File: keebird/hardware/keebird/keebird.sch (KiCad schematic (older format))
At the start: 2 parts

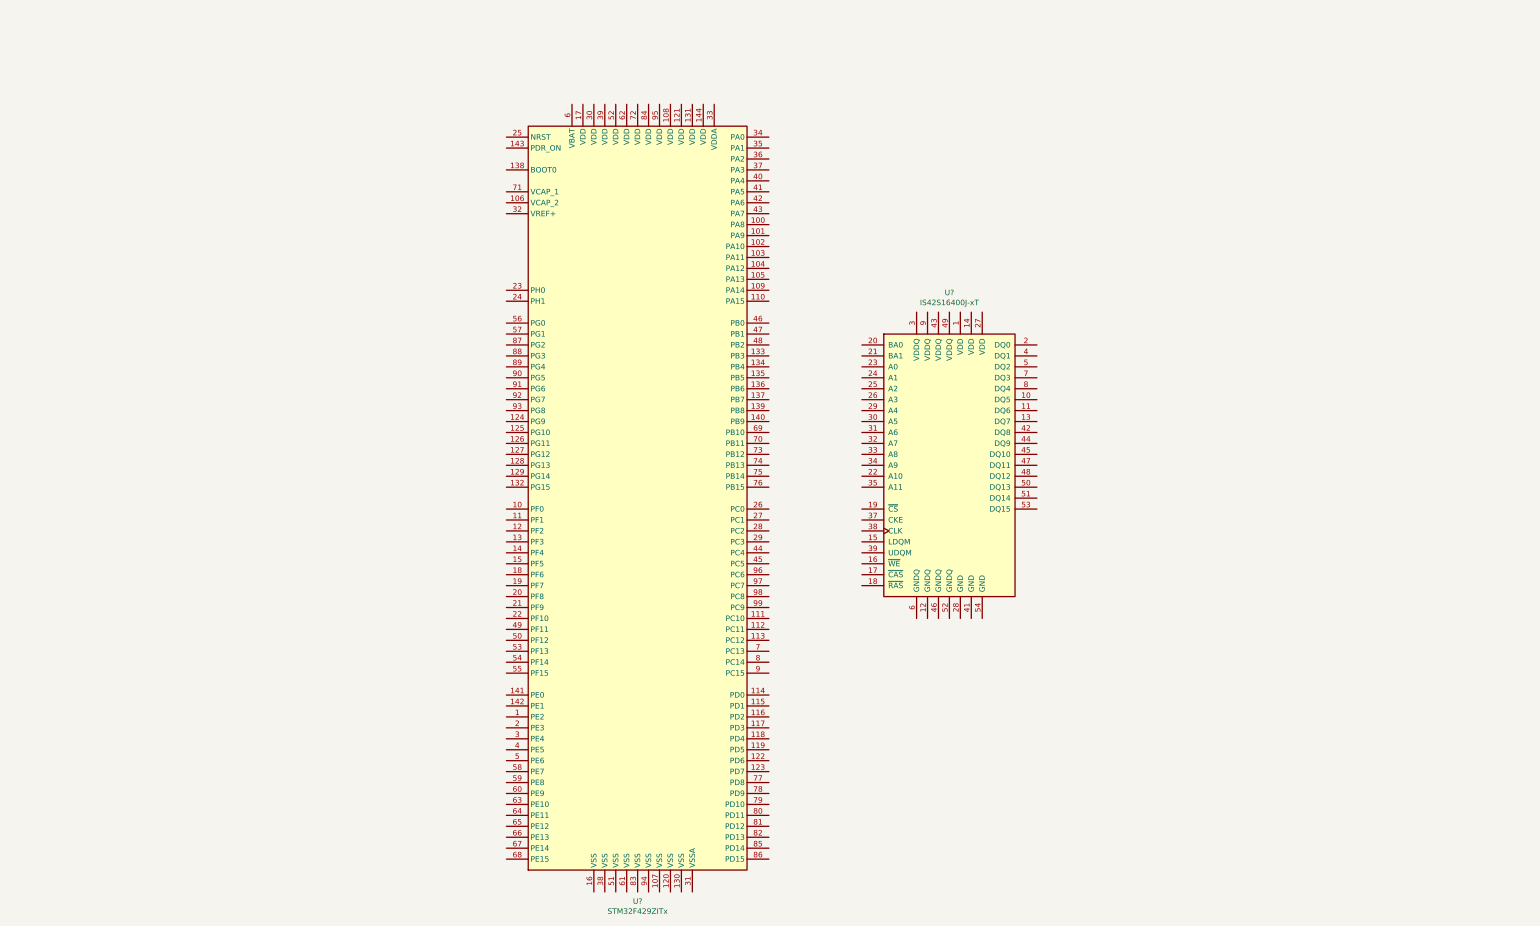
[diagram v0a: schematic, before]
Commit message: Add address and data pin connections for RAM.
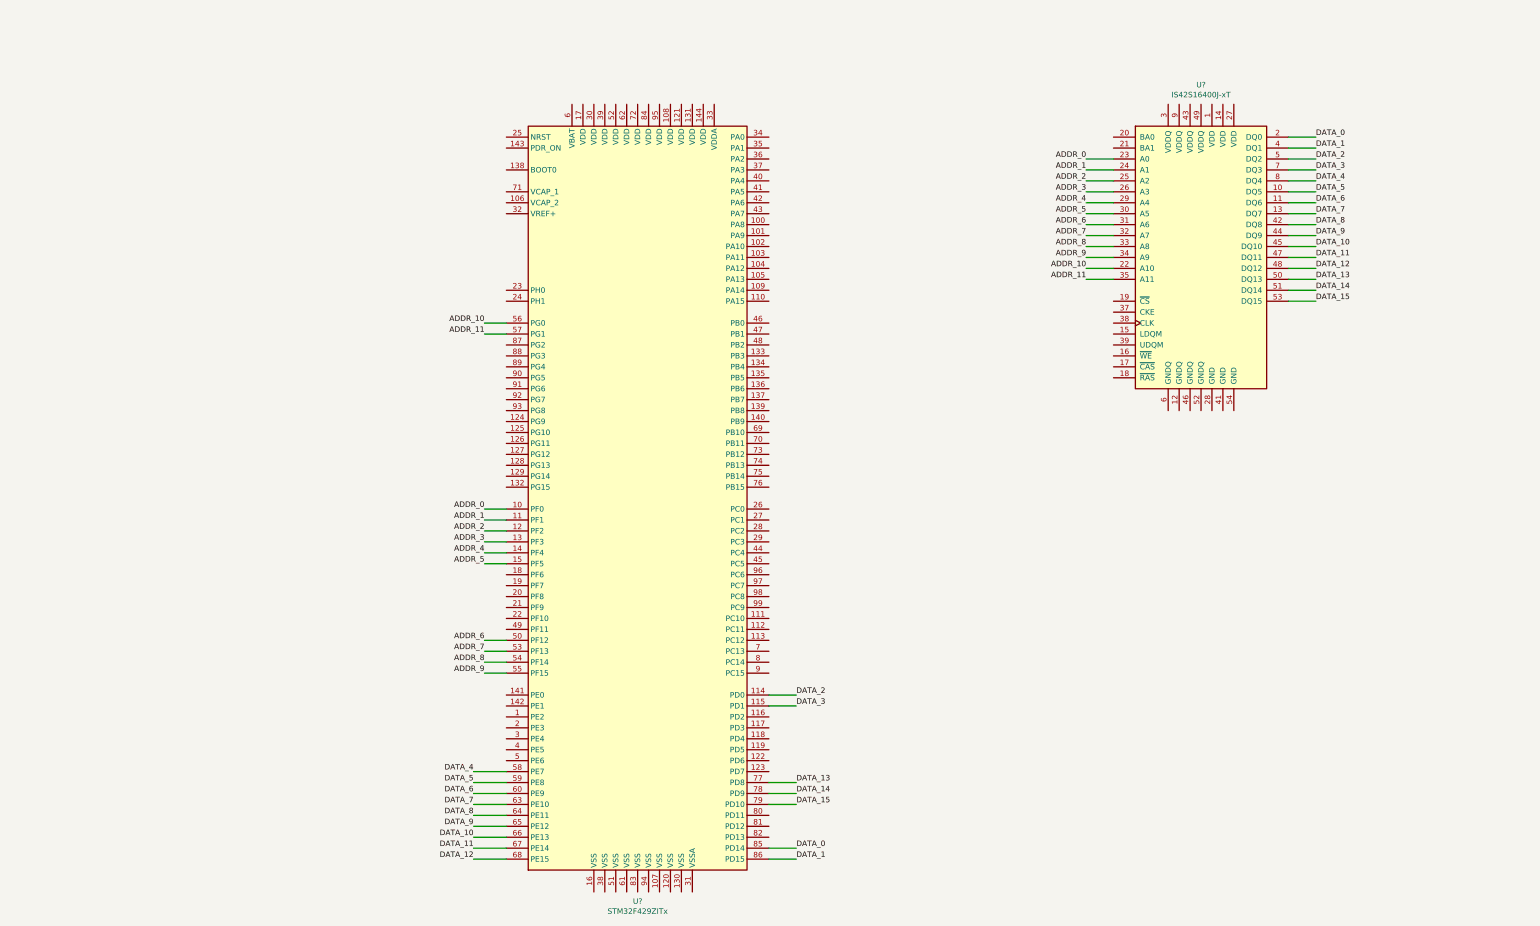
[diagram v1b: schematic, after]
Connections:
- net ADDR_0: now reaches U?.10 (PF0)
- net ADDR_0: now also U?.23 (A0)
- net ADDR_1: now reaches U?.11 (PF1)
- net ADDR_1: now also U?.24 (A1)
- net DATA_2: now reaches U?.114 (PD0)
- net DATA_2: now also U?.5 (DQ2)
- net DATA_3: now reaches U?.115 (PD1)
- net DATA_3: now also U?.7 (DQ3)
- net ADDR_2: now reaches U?.12 (PF2)
- net ADDR_2: now also U?.25 (A2)
- net ADDR_3: now reaches U?.13 (PF3)
- net ADDR_3: now also U?.26 (A3)
- net ADDR_4: now reaches U?.14 (PF4)
- net ADDR_4: now also U?.29 (A4)
- net ADDR_5: now reaches U?.15 (PF5)
- net ADDR_5: now also U?.30 (A5)
- net ADDR_6: now reaches U?.50 (PF12)
- net ADDR_6: now also U?.31 (A6)
- net ADDR_7: now reaches U?.53 (PF13)
- net ADDR_7: now also U?.32 (A7)
- net ADDR_8: now reaches U?.54 (PF14)
- net ADDR_8: now also U?.33 (A8)
- net ADDR_9: now reaches U?.55 (PF15)
- net ADDR_9: now also U?.34 (A9)
- net ADDR_10: now reaches U?.56 (PG0)
- net ADDR_10: now also U?.22 (A10)
- net ADDR_11: now reaches U?.57 (PG1)
- net ADDR_11: now also U?.35 (A11)
- net DATA_4: now reaches U?.58 (PE7)
- net DATA_4: now also U?.8 (DQ4)
- net DATA_5: now reaches U?.59 (PE8)
- net DATA_5: now also U?.10 (DQ5)
- net DATA_6: now reaches U?.60 (PE9)
- net DATA_6: now also U?.11 (DQ6)
- net DATA_7: now reaches U?.63 (PE10)
- net DATA_7: now also U?.13 (DQ7)
- net DATA_8: now reaches U?.64 (PE11)
- net DATA_8: now also U?.42 (DQ8)
- net DATA_9: now reaches U?.65 (PE12)
- net DATA_9: now also U?.44 (DQ9)
- net DATA_10: now reaches U?.66 (PE13)
- net DATA_10: now also U?.45 (DQ10)
- net DATA_11: now reaches U?.67 (PE14)
- net DATA_11: now also U?.47 (DQ11)
- net DATA_12: now reaches U?.68 (PE15)
- net DATA_12: now also U?.48 (DQ12)
- net DATA_13: now reaches U?.77 (PD8)
- net DATA_13: now also U?.50 (DQ13)
- net DATA_14: now reaches U?.78 (PD9)
- net DATA_14: now also U?.51 (DQ14)
- net DATA_15: now reaches U?.79 (PD10)
- net DATA_15: now also U?.53 (DQ15)
- net DATA_0: now reaches U?.85 (PD14)
- net DATA_0: now also U?.2 (DQ0)
- net DATA_1: now reaches U?.86 (PD15)
- net DATA_1: now also U?.4 (DQ1)
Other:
- moved on the sheet: U?
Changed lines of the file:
@@
 L Memory_RAM:IS42S16400J-xT U?
 U 1 1 5B786488
-P 9900 4650
-F 0 "U?" H 9900 6228 50  0000 C CNN
-F 1 "IS42S16400J-xT" H 9900 6137 50  0000 C CNN
-F 2 "Package_SO:TSOP-II-54_10.16x22.22mm_P0.8mm" H 9900 4650 50  0001 C CNN
-F 3 "http://www.issi.com/WW/pdf/42-45S16400J.pdf" H 9300 5900 50  0001 C CNN
-	1    9900 4650
+P 12200 2750
+F 0 "U?" H 12200 4328 50  0000 C CNN
+F 1 "IS42S16400J-xT" H 12200 4237 50  0000 C CNN
+F 2 "Package_SO:TSOP-II-54_10.16x22.22mm_P0.8mm" H 12200 2750 50  0001 C CNN
+F 3 "http://www.issi.com/WW/pdf/42-45S16400J.pdf" H 11600 4000 50  0001 C CNN
+	1    12200 2750
 	1    0    0    -1
 $EndComp
+Wire Wire Line
+	11400 1850 11150 1850
+Text Label 11150 1850 2    50   ~ 0
+ADDR_0
+Wire Wire Line
+	11400 1950 11150 1950
+Text Label 11150 1950 2    50   ~ 0
+ADDR_1
+Wire Wire Line
+	11150 2050 11400 2050
+Text Label 11150 2050 2    50   ~ 0
+ADDR_2
+Wire Wire Line
+	11400 2150 11150 2150
+Text Label 11150 2150 2    50   ~ 0
+ADDR_3
+Wire Wire Line
+	11400 2250 11150 2250
+Text Label 11150 2250 2    50   ~ 0
+ADDR_4
+Wire Wire Line
+	11400 2350 11150 2350
+Text Label 11150 2350 2    50   ~ 0
+ADDR_5
+Wire Wire Line
+	11400 2450 11150 2450
+Text Label 11150 2450 2    50   ~ 0
+ADDR_6
+Wire Wire Line
+	11400 2550 11150 2550
+Text Label 11150 2550 2    50   ~ 0
+ADDR_7
+Wire Wire Line
+	11400 2650 11150 2650
+Text Label 11150 2650 2    50   ~ 0
+ADDR_8
+Wire Wire Line
+	11400 2750 11150 2750
+Text Label 11150 2750 2    50   ~ 0
+ADDR_9
+Wire Wire Line
+	11400 2850 11150 2850
+Text Label 11150 2850 2    50   ~ 0
+ADDR_10
+Wire Wire Line
+	11400 2950 11150 2950
+Text Label 11150 2950 2    50   ~ 0
+ADDR_11
+Wire Wire Line
+	5850 5050 5650 5050
+Text Label 5650 5050 2    50   ~ 0
+ADDR_0
+Wire Wire Line
+	5850 5150 5650 5150
+Text Label 5650 5150 2    50   ~ 0
+ADDR_1
+Wire Wire Line
+	5850 5250 5650 5250
+Text Label 5650 5250 2    50   ~ 0
+ADDR_2
+Wire Wire Line
+	5850 5350 5650 5350
+Text Label 5650 5350 2    50   ~ 0
+ADDR_3
+Wire Wire Line
+	5850 5450 5650 5450
+Text Label 5650 5450 2    50   ~ 0
+ADDR_4
+Wire Wire Line
+	5850 5550 5650 5550
+Text Label 5650 5550 2    50   ~ 0
+ADDR_5
+Wire Wire Line
+	5850 6250 5650 6250
+Text Label 5650 6250 2    50   ~ 0
+ADDR_6
+Wire Wire Line
+	5850 6350 5650 6350
+Text Label 5650 6350 2    50   ~ 0
+ADDR_7
+Wire Wire Line
+	5850 6450 5650 6450
+Text Label 5650 6450 2    50   ~ 0
+ADDR_8
+Wire Wire Line
+	5850 6550 5650 6550
+Text Label 5650 6550 2    50   ~ 0
+ADDR_9
+Wire Wire Line
+	5850 3350 5650 3350
+Text Label 5650 3350 2    50   ~ 0
+ADDR_10
+Wire Wire Line
+	5850 3450 5650 3450
+Text Label 5650 3450 2    50   ~ 0
+ADDR_11
+Wire Wire Line
+	13000 1650 13250 1650
+Text Label 13250 1650 0    50   ~ 0
+DATA_0
+Wire Wire Line
+	13000 1750 13250 1750
+Text Label 13250 1750 0    50   ~ 0
+DATA_1
+Wire Wire Line
+	13000 1850 13250 1850
+Text Label 13250 1850 0    50   ~ 0
+DATA_2
+Wire Wire Line
+	13000 1950 13250 1950
+Text Label 13250 1950 0    50   ~ 0
+DATA_3
+Wire Wire Line
+	13000 2050 13250 2050
+Text Label 13250 2050 0    50   ~ 0
+DATA_4
+Wire Wire Line
+	13000 2150 13250 2150
+Text Label 13250 2150 0    50   ~ 0
+DATA_5
+Wire Wire Line
+	13000 2250 13250 2250
+Text Label 13250 2250 0    50   ~ 0
+DATA_6
+Wire Wire Line
+	13000 2350 13250 2350
+Text Label 13250 2350 0    50   ~ 0
+DATA_7
+Wire Wire Line
+	13000 2450 13250 2450
+Text Label 13250 2450 0    50   ~ 0
+DATA_8
+Wire Wire Line
+	13000 2550 13250 2550
+Text Label 13250 2550 0    50   ~ 0
+DATA_9
+Wire Wire Line
+	13000 2650 13250 2650
+Text Label 13250 2650 0    50   ~ 0
+DATA_10
+Wire Wire Line
+	13000 2750 13250 2750
+Text Label 13250 2750 0    50   ~ 0
+DATA_11
+Wire Wire Line
+	13000 2850 13250 2850
+Text Label 13250 2850 0    50   ~ 0
+DATA_12
+Wire Wire Line
+	13000 2950 13250 2950
+Text Label 13250 2950 0    50   ~ 0
+DATA_13
+Wire Wire Line
+	13000 3050 13250 3050
+Text Label 13250 3050 0    50   ~ 0
+DATA_14
+Wire Wire Line
+	13000 3150 13250 3150
+Text Label 13250 3150 0    50   ~ 0
+DATA_15
+Wire Wire Line
+	8250 8150 8500 8150
+Text Label 8500 8150 0    50   ~ 0
+DATA_0
+Wire Wire Line
+	8250 8250 8500 8250
+Text Label 8500 8250 0    50   ~ 0
+DATA_1
+Wire Wire Line
+	8250 6750 8500 6750
+Text Label 8500 6750 0    50   ~ 0
+DATA_2
+Wire Wire Line
+	8250 6850 8500 6850
+Text Label 8500 6850 0    50   ~ 0
+DATA_3
+Wire Wire Line
+	5850 7450 5550 7450
+Text Label 5550 7450 2    50   ~ 0
+DATA_4
+Wire Wire Line
+	5850 7550 5550 7550
+Text Label 5550 7550 2    50   ~ 0
+DATA_5
+Wire Wire Line
+	5850 7650 5550 7650
+Text Label 5550 7650 2    50   ~ 0
+DATA_6
+Wire Wire Line
+	5850 7750 5550 7750
+Text Label 5550 7750 2    50   ~ 0
+DATA_7
+Wire Wire Line
+	5850 7850 5550 7850
+Text Label 5550 7850 2    50   ~ 0
+DATA_8
+Wire Wire Line
+	5850 7950 5550 7950
+Text Label 5550 7950 2    50   ~ 0
+DATA_9
+Wire Wire Line
+	5850 8050 5550 8050
+Text Label 5550 8050 2    50   ~ 0
+DATA_10
+Wire Wire Line
+	5850 8150 5550 8150
+Text Label 5550 8150 2    50   ~ 0
+DATA_11
+Wire Wire Line
+	5850 8250 5550 8250
+Text Label 5550 8250 2    50   ~ 0
+DATA_12
+Wire Wire Line
+	8250 7550 8500 7550
+Text Label 8500 7550 0    50   ~ 0
+DATA_13
+Wire Wire Line
+	8250 7650 8500 7650
+Text Label 8500 7650 0    50   ~ 0
+DATA_14
+Wire Wire Line
+	8250 7750 8500 7750
+Text Label 8500 7750 0    50   ~ 0
+DATA_15
 $EndSCHEMATC

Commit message: Finish wiring RAM.
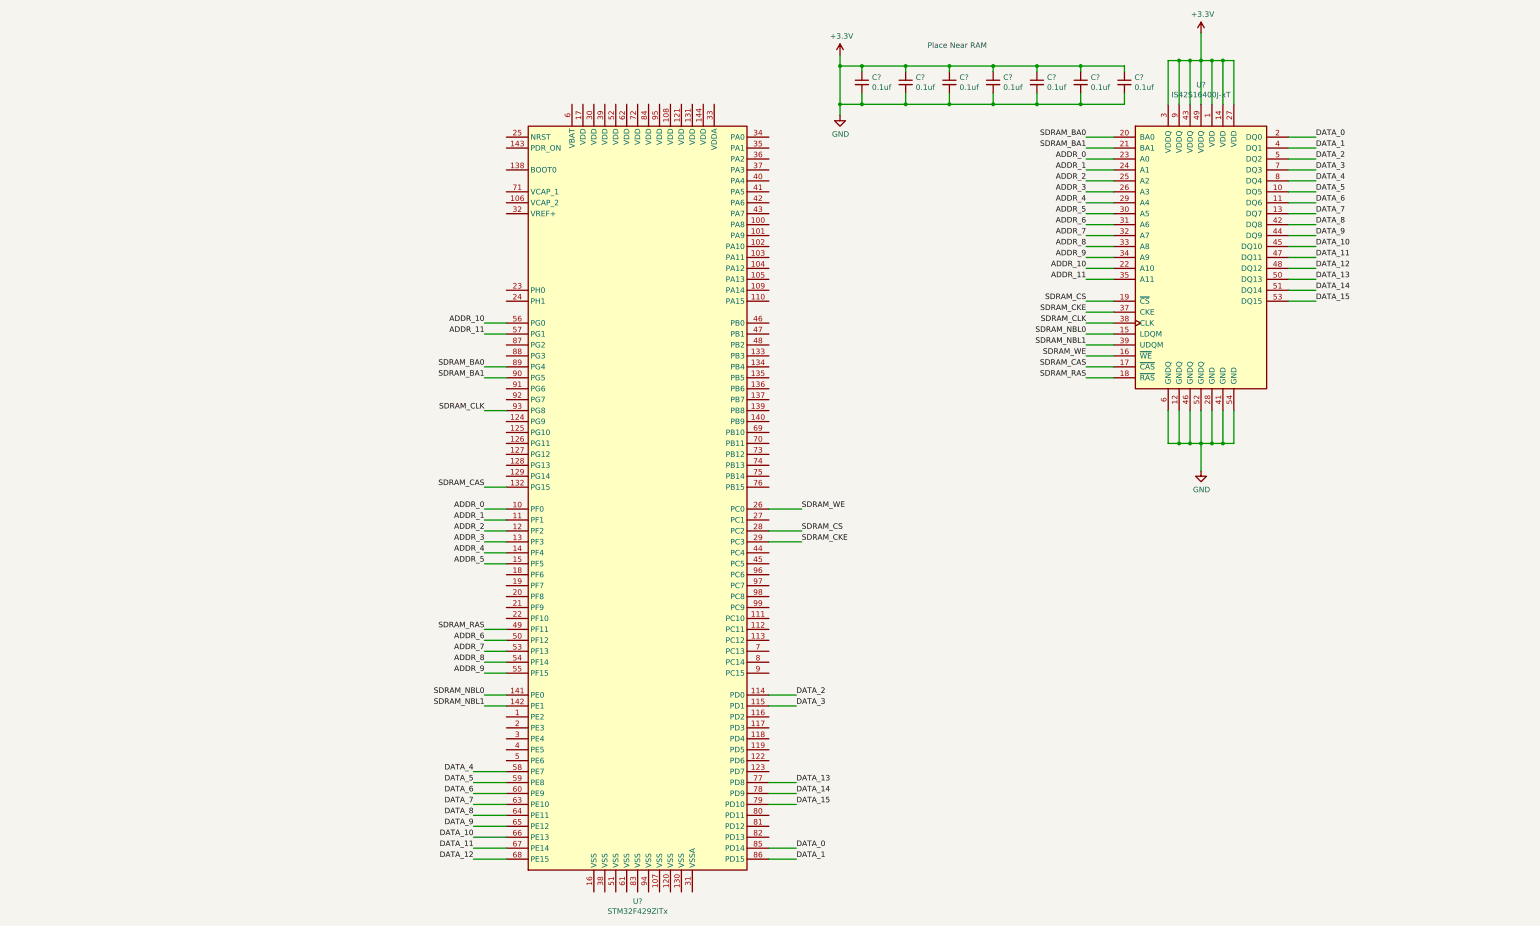
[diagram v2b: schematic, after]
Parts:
- added C? (x7): 0.1uf, symbol Device:C_Small
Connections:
- net SDRAM_CAS: now reaches U?.132 (PG15)
- net SDRAM_CAS: now also U?.17 (~CAS)
- net SDRAM_NBL0: now reaches U?.141 (PE0)
- net SDRAM_NBL0: now also U?.15 (LDQM)
- net SDRAM_NBL1: now reaches U?.142 (PE1)
- net SDRAM_NBL1: now also U?.39 (UDQM)
- net SDRAM_WE: now reaches U?.26 (PC0)
- net SDRAM_WE: now also U?.16 (~WE)
- net SDRAM_CS: now reaches U?.28 (PC2)
- net SDRAM_CS: now also U?.19 (~CS)
- net SDRAM_CKE: now reaches U?.29 (PC3)
- net SDRAM_CKE: now also U?.37 (CKE)
- net SDRAM_RAS: now reaches U?.49 (PF11)
- net SDRAM_RAS: now also U?.18 (~RAS)
- net SDRAM_BA0: now reaches U?.89 (PG4)
- net SDRAM_BA0: now also U?.20 (BA0)
- net SDRAM_BA1: now reaches U?.90 (PG5)
- net SDRAM_BA1: now also U?.21 (BA1)
- net SDRAM_CLK: now reaches U?.93 (PG8)
- net SDRAM_CLK: now also U?.38 (CLK)
- net +3V3: now reaches U?.1 (VDD)
- net +3V3: now also U?.12 (GNDQ), U?.14 (VDD), U?.27 (VDD), U?.28 (GND), U?.3 (VDDQ), U?.41 (GND), U?.43 (VDDQ), U?.46 (GNDQ), U?.49 (VDDQ), U?.52 (GNDQ), U?.54 (GND), U?.6 (GNDQ), U?.9 (VDDQ), C?.1, C?.1, C?.1, C?.1, C?.1, C?.1, C?.1, C?.2, C?.2, C?.2, C?.2, C?.2, C?.2, C?.2
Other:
- note added: "Place Near RAM\n"
